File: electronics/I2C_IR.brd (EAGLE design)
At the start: 13 x 19.9 mm, 10 parts, among them U1 ADC081C021

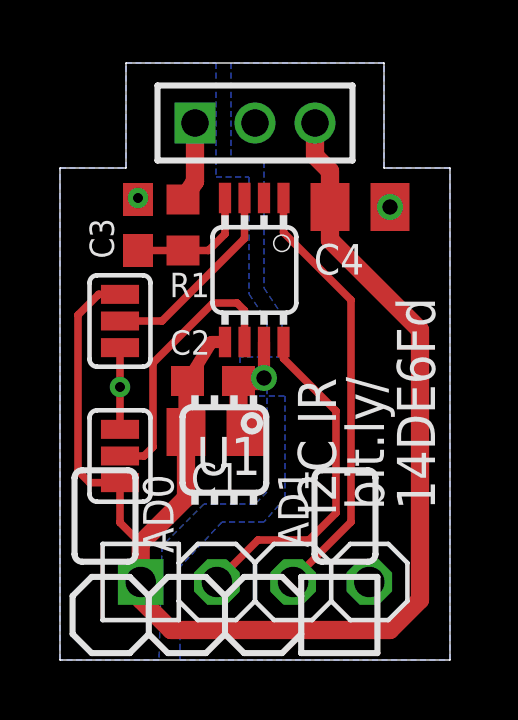
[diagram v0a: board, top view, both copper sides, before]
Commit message: Revised board layout removing 'cut' per white paper I read.
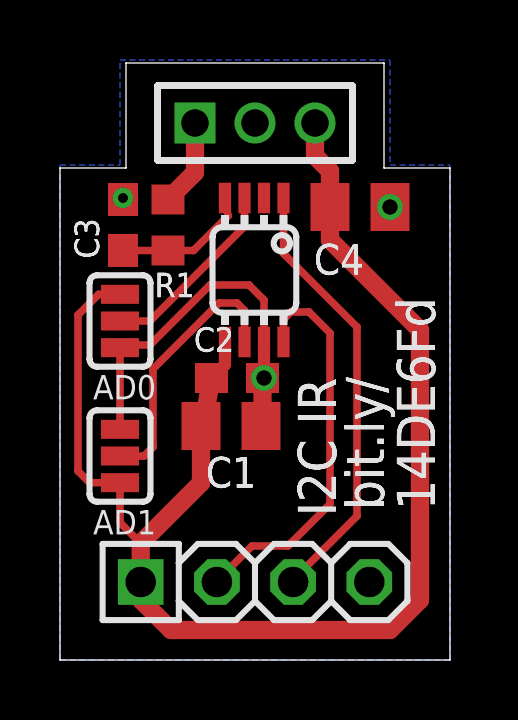
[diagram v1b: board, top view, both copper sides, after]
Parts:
- moved C2 0.81 mm to (5.90, 9.40)
- moved C1 0.54 mm to (5.70, 7.80)
- moved C3 0.50 mm to (2.10, 14.5)
- moved R1 0.50 mm to (3.60, 14.5)
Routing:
- net GND: track 6.78 -> 13.2 mm, vias 4 -> 3
- net SDA: track 11.4 -> 13.3 mm
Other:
- board text added: "C1"
- board text added: "C2"
- board text added: "C3"
- board text added: "C4"
- board text added: "R1"
- board text removed: "I2CIR"
- board text removed: "U1"
- board text removed: "bot-thoughts.com"
